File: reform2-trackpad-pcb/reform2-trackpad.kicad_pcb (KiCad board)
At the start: 2 copper layers, 45 x 21 mm, 22 parts, among them J1 Conn_USB, J2 Conn_01x06_Female, SW6 SW_RST, SW7 SW_HWB, U1 ATmega32U2-AU, U2 TLV75533PDBV, Y1 Crystal_GND24

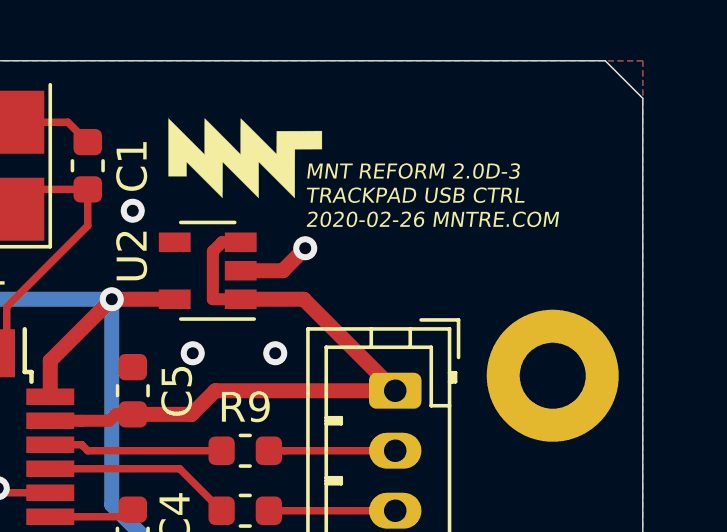
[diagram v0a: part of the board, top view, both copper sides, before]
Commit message: WIP trackpad now CERN-OHL-S 2.0
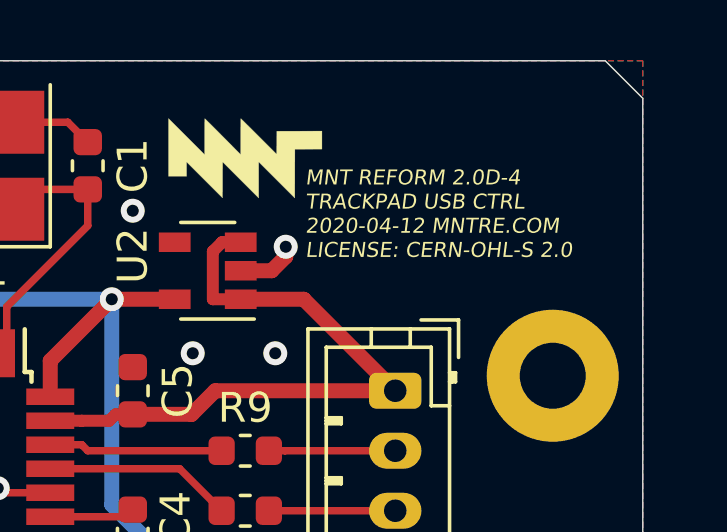
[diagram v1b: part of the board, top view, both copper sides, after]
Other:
- board text added: "MNT REFORM 2.0D-4 TRACKPAD USB CTRL 2020-04-12 MNTRE.COM LICENSE: CERN-OHL-S 2.0"
- board text removed: "MNT REFORM 2.0D-3 TRACKPAD USB CTRL 2020-02-26 MNTRE.COM"
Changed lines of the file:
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@@
-(kicad_pcb (version 20171130) (host pcbnew 5.1.2+dfsg1-1)
+(kicad_pcb (version 20171130) (host pcbnew 5.1.5+dfsg1-2+b1)
   (general
     (thickness 1.6)
     (drawings 12)
-    (tracks 143)
+    (tracks 144)
     (zones 0)
     (modules 22)
@@
   (gr_line (start 174.75 95) (end 217.25 95) (layer Edge.Cuts) (width 0.05))
   (gr_line (start 173.5 106.5) (end 173.5 96.25) (layer Edge.Cuts) (width 0.05))
-  (gr_text "MNT REFORM 2.0D-3\nTRACKPAD USB CTRL\n2020-02-26 MNTRE.COM" (at 207.25 99.5) (layer F.SilkS)
+  (gr_text "MNT REFORM 2.0D-4\nTRACKPAD USB CTRL\n2020-04-12 MNTRE.COM\nLICENSE: CERN-OHL-S 2.0" (at 207.25 100.1) (layer F.SilkS)
     (effects (font (size 0.5 0.5) (thickness 0.1) italic) (justify left))
   )
@@
   (via (at 203.5 104.75) (size 0.8) (drill 0.4) (layers F.Cu B.Cu) (net 1))
   (via (at 206.25 104.75) (size 0.8) (drill 0.4) (layers F.Cu B.Cu) (net 1))
-  (via (at 207.25 101.25) (size 0.8) (drill 0.4) (layers F.Cu B.Cu) (net 1))
-  (segment (start 206.5 102) (end 207.25 101.25) (width 0.5) (layer F.Cu) (net 1))
-  (segment (start 205.1 102) (end 206.5 102) (width 0.5) (layer F.Cu) (net 1))
   (via (at 194.75 109.25) (size 0.8) (drill 0.4) (layers F.Cu B.Cu) (net 1))
   (via (at 193.5 107.75) (size 0.8) (drill 0.4) (layers F.Cu B.Cu) (net 1))
@@
   (segment (start 201.5 111.5375) (end 200.5375 111.5375) (width 0.25) (layer F.Cu) (net 1))
   (segment (start 200.5375 111.5375) (end 200.5 111.5) (width 0.25) (layer F.Cu) (net 1))
+  (via (at 206.6 101.2) (size 0.8) (drill 0.4) (layers F.Cu B.Cu) (net 1))
+  (segment (start 205.1 102) (end 206.13 102) (width 0.5) (layer F.Cu) (net 1))
+  (segment (start 206.13 102) (end 206.6 101.53) (width 0.5) (layer F.Cu) (net 1))
+  (segment (start 206.6 101.53) (end 206.6 101.2) (width 0.5) (layer F.Cu) (net 1))
   (segment (start 200 99.2875) (end 200 100.5) (width 0.25) (layer F.Cu) (net 2))
   (segment (start 197.3 103.2) (end 197.3 104.75) (width 0.25) (layer F.Cu) (net 2))

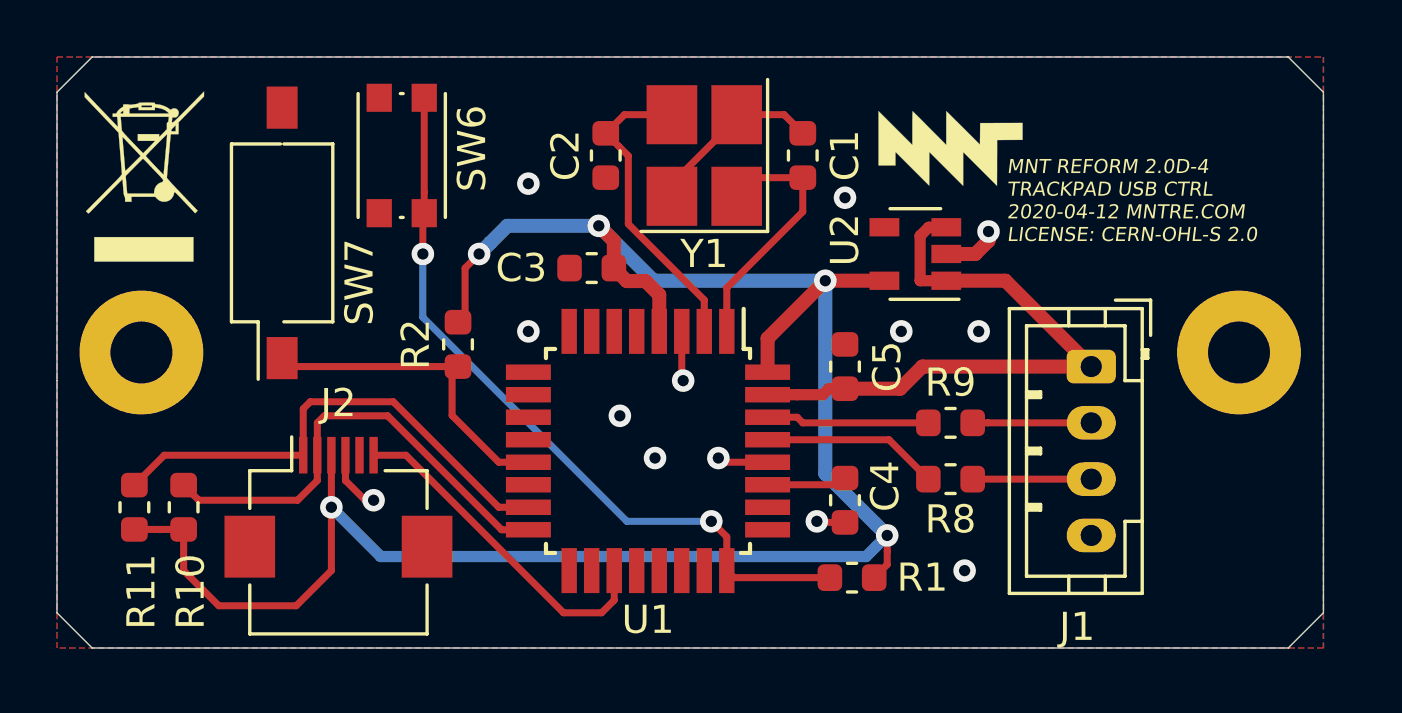
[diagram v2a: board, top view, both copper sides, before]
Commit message: trackpad: add ESD protection and fuse, add badge, bump to R-1
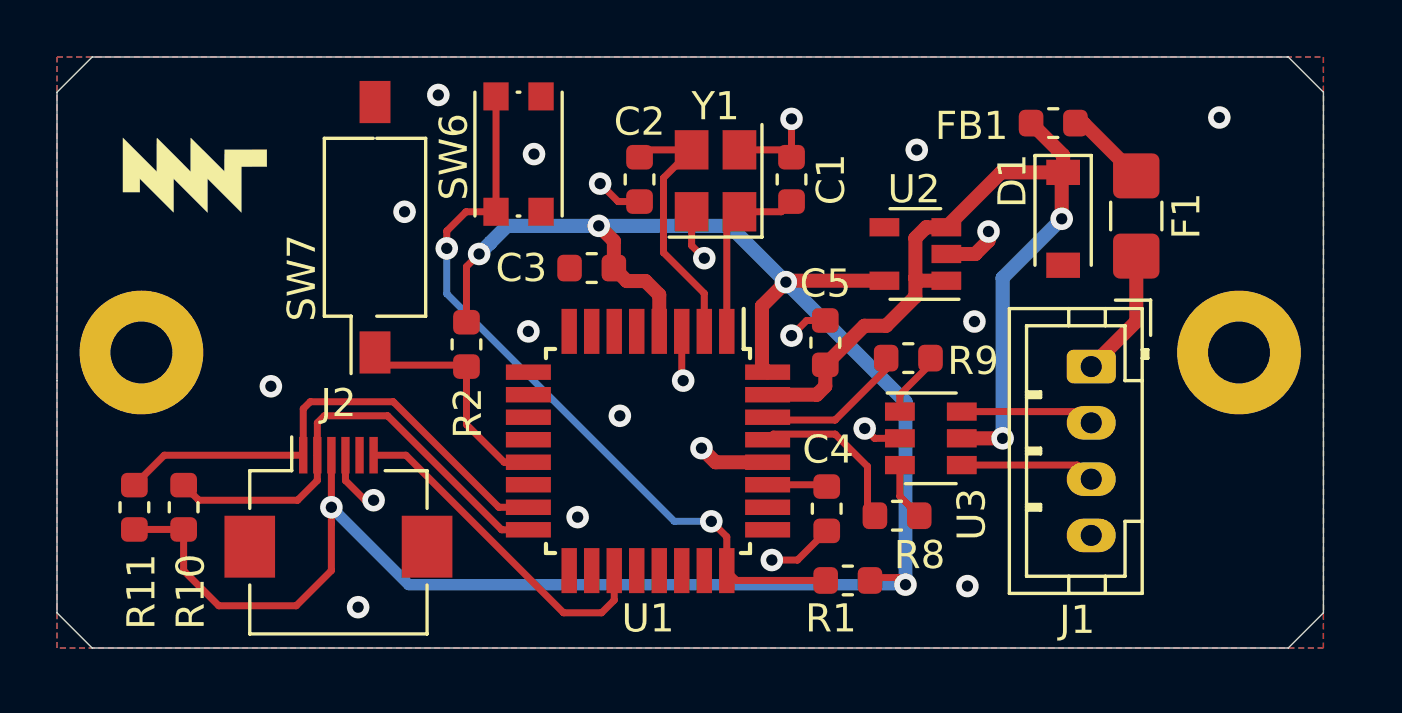
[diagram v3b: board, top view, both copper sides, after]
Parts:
- added D1: BZT52-B5V6J, Diode_SMD:D_SOD-123, F.Cu at (209.2, 100.8)
- added F1: 0ZCJ0075AF2E, Fuse:Fuse_1206_3216Metric_Castellated, F.Cu at (211.8, 100.7)
- added FB1: BLM18PG221SH1D, Inductor_SMD:L_0603_1608Metric, F.Cu at (208.9, 97.3)
- added U3: USBLC6-2SC6, Package_TO_SOT_SMD:SOT-23-6, F.Cu at (204.6, 108.5)
- MK1: value WEEE -> BADGE; footprint Symbol:WEEE-Logo_4.2x6mm_SilkScreen -> footprints:reform2-trackpadctrl-badge; moved to B.Cu
- Y1: footprint Crystal:Crystal_SMD_3225-4Pin_3.2x2.5mm_HandSoldering -> Crystal:Crystal_SMD_3225-4Pin_3.2x2.5mm
- moved MK13 26.9 mm to (178.4, 99.2)
- moved MK1 18.5 mm to (193.9, 105.9)
- moved SW6 4.15 mm to (189.9, 98.5), turned to 270 degrees
- moved SW7 3.31 mm to (184.8, 101.0)
- moved R9 2.75 mm to (203.8, 105.7)
- moved R8 2.30 mm to (203.3, 111.3)
- moved C2 1.47 mm to (194.2, 99.3)
- moved C5 1.10 mm to (200.8, 105.2)
- moved Y1 0.98 mm to (196.9, 99.4)
- moved C1 0.94 mm to (199.6, 99.3)
- moved C4 0.72 mm to (200.8, 111.0)
- moved R2 0.30 mm to (188.1, 105.2)
- moved R1 0.18 mm to (201.6, 113.6)
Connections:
- J1 pad 1: +5V -> /5V_IN
- J1 pad 2: Net-(J1-Pad2) -> /PD-
- J1 pad 3: Net-(J1-Pad3) -> /PD+
- R8 pad 1: Net-(J1-Pad3) -> /UD+
- R9 pad 2: Net-(J1-Pad2) -> /UD-
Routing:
- net +5V: track 21.9 -> 30.6 mm, vias 0 -> 2
- net GND: track 15.3 -> 20.6 mm, vias 13 -> 22
- net /PD+: track 0.00 -> 4.81 mm
- net /PD-: track 0.00 -> 4.77 mm
- net /5V_IN: track 0.00 -> 4.59 mm
- net Net-(J1-Pad3): track 4.21 -> 0.00 mm
- net Net-(J1-Pad2): track 4.21 -> 0.00 mm
- net Net-(R2-Pad1): track 11.9 -> 8.27 mm
- net Net-(F1-Pad1): track 0.00 -> 2.94 mm
- net Net-(C1-Pad1): track 9.21 -> 6.44 mm
- net +3V3: track 73.2 -> 75.8 mm
- net /UD-: track 0.00 -> 2.35 mm
- net /UD+: track 0.00 -> 2.08 mm
- net Net-(C2-Pad2): track 11.1 -> 9.42 mm
- net Net-(C4-Pad1): track 3.10 -> 2.13 mm
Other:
- board text removed: "MNT REFORM 2.0D-4 TRACKPAD USB CTRL 2020-04-12 MNTRE.COM LICENSE: CERN-OHL-S 2.0"
